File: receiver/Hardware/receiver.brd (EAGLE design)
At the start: 70 x 21 mm, 17 parts, among them IC2 MEGA8-P, Q1 16 MHz, X1 USB-A-H

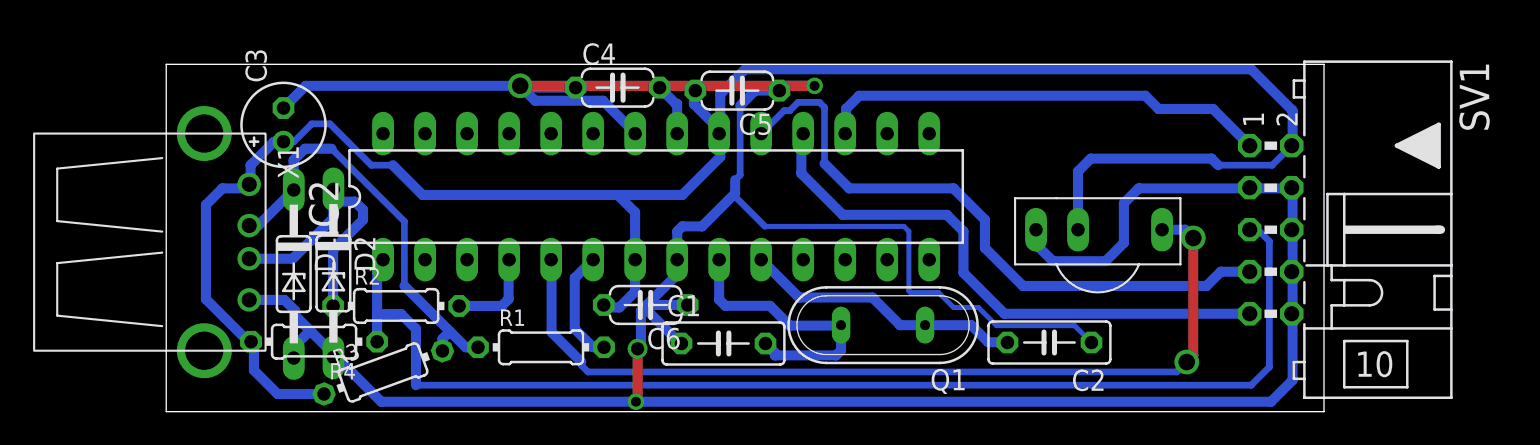
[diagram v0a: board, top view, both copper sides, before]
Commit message: Naprawa schematu
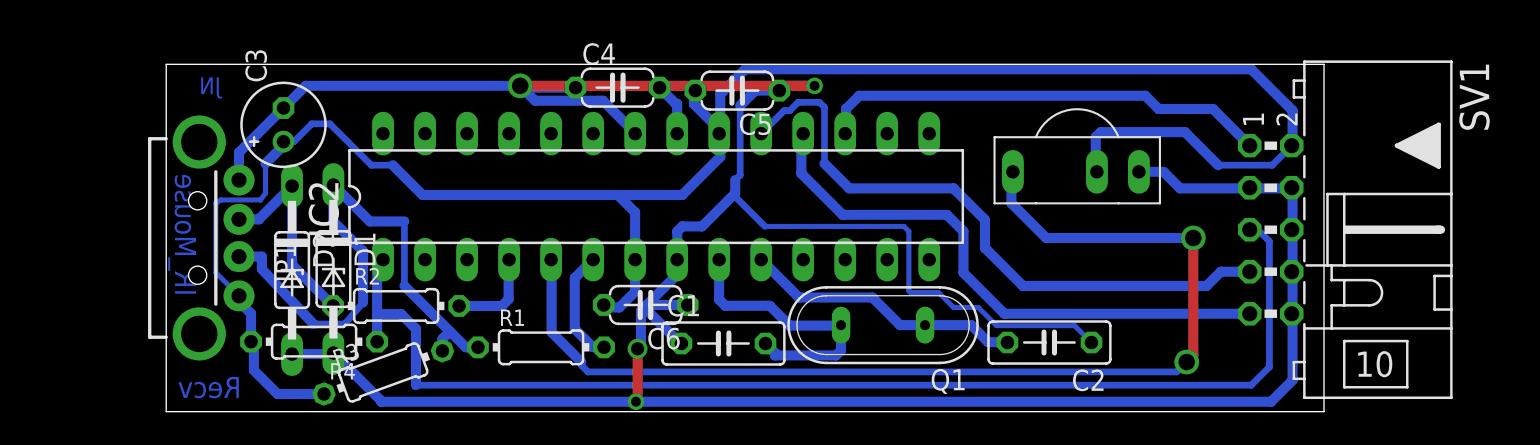
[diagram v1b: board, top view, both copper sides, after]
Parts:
- removed X1: USB-A-H, con-usb:USB-A-H
- added JP1: USB-A-H, SparkFun-Connectors:USB-A-H
- moved TSOP1 3.77 mm to (55.0, 13.5), turned to 180 degrees
- moved D2 2.51 mm to (7.61, 7.56)
- moved D1 2.42 mm to (10.1, 7.62)
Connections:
- net D+: now also JP1.D+; no longer X1.D+
- net D-: now also JP1.D-; no longer X1.D-
- net GND: now also JP1.GND; no longer X1.GND
- net VBUS: now also JP1.VBUS; no longer X1.VBUS
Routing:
- net IR_OUT: track 53.9 -> 65.6 mm
- net GND: track 203.9 -> 192.7 mm
- net D-: track 27.0 -> 34.6 mm
- net D+: track 17.1 -> 12.3 mm
- net VBUS: track 124.9 -> 122.1 mm
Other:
- board text added: "IR_Mouse"
- board text added: "JN"
- board text added: "Recv"
